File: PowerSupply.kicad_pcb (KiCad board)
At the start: 2 copper layers, 15 parts, among them J1 Barrel_Jack_Switch, J2 Conn_02x02_Odd_Even, J3 Conn_02x02_Odd_Even, SW1 SW_DPDT_x2, U1 LM7805_TO220

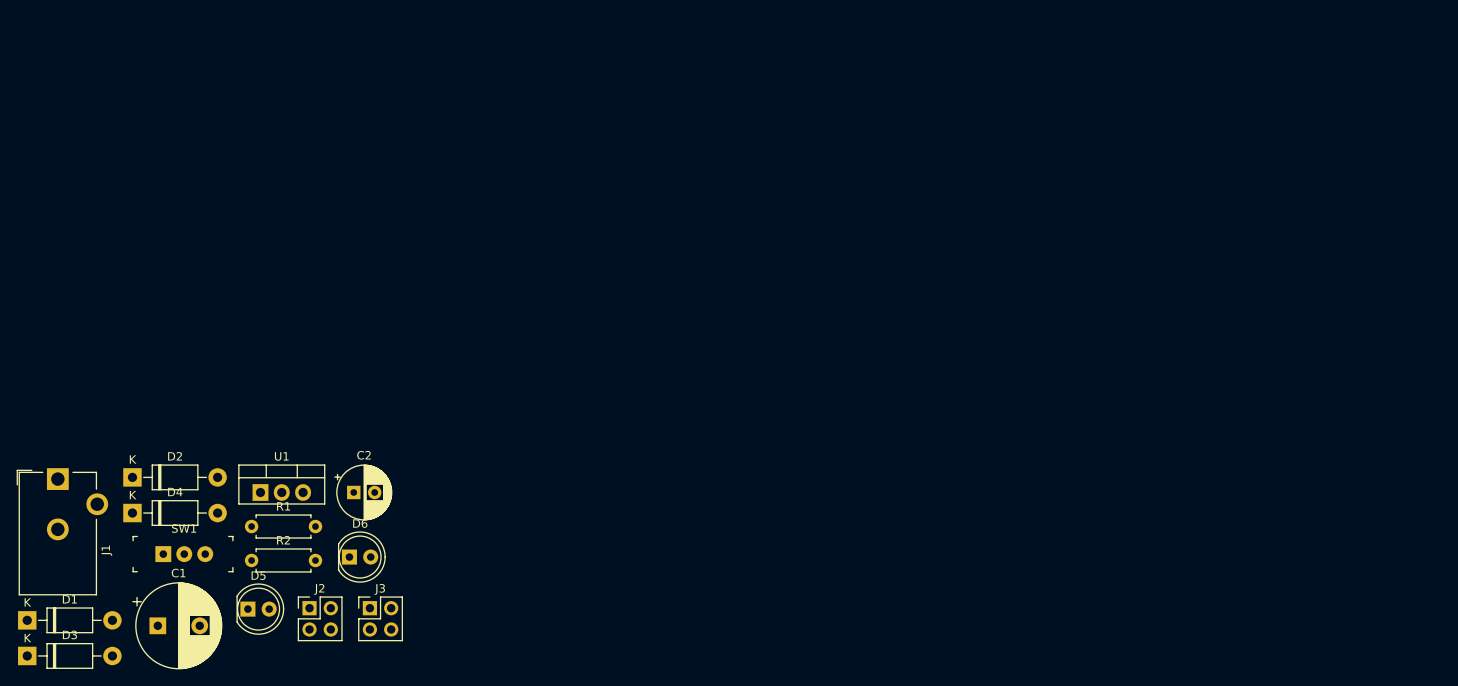
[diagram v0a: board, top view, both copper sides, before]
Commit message: Drew outline and constraints of the pcb
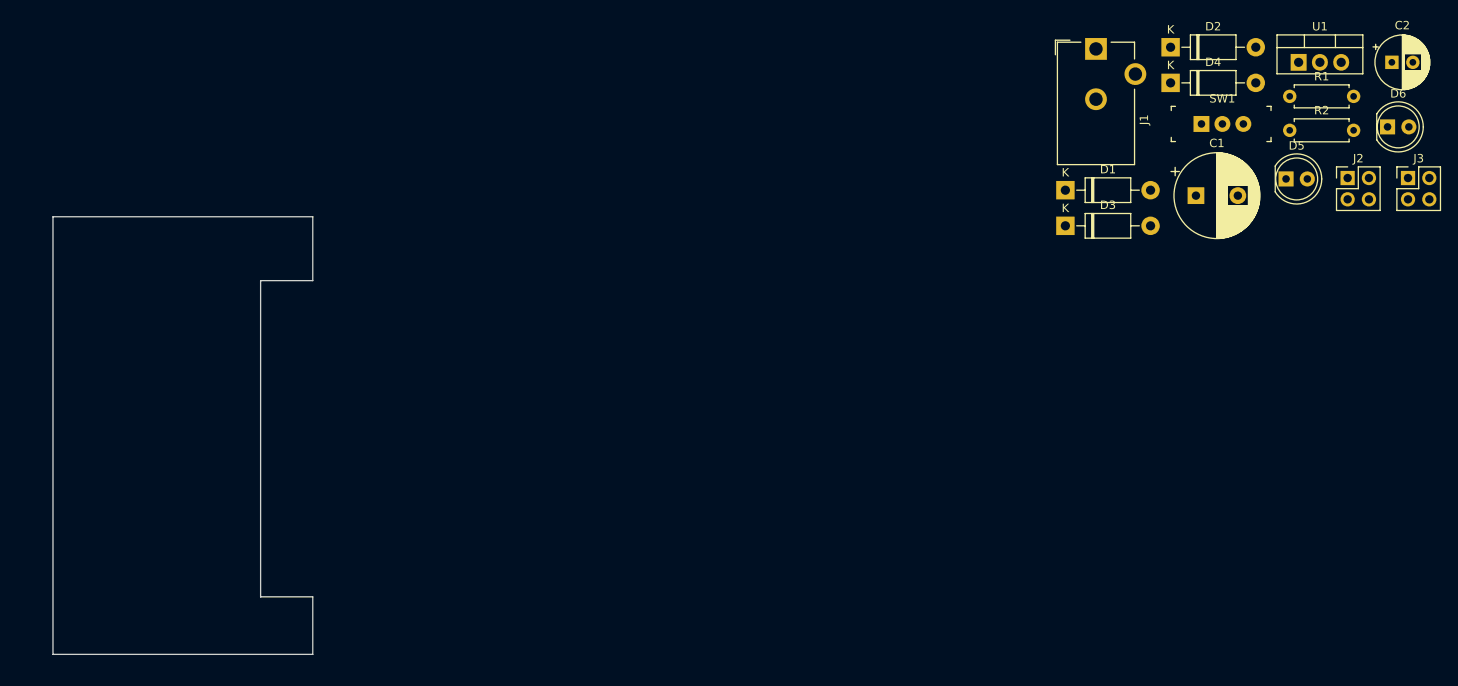
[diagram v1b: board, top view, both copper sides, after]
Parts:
- moved J2 134.0 mm to (256.4, 71.6)
- moved C1 134.0 mm to (238.3, 73.7)
- moved C2 134.0 mm to (261.7, 57.8)
- moved D1 134.0 mm to (222.7, 73.0)
- moved D2 134.0 mm to (235.3, 56.0)
- moved D3 134.0 mm to (222.7, 77.3)
- moved D4 134.0 mm to (235.3, 60.2)
- moved D5 134.0 mm to (249.1, 71.7)
- moved D6 134.0 mm to (261.2, 65.5)
- moved J1 134.0 mm to (226.4, 56.2)
- moved J3 134.0 mm to (263.6, 71.6)
- moved R1 134.0 mm to (249.5, 61.8)
- moved R2 134.0 mm to (249.5, 65.9)
- moved SW1 134.0 mm to (239.0, 65.1)
- moved U1 134.0 mm to (250.6, 57.8)
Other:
- board outline added: 31 x 52.2 mm
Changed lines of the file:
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@@
   (general
     (thickness 1.6)
-    (drawings 0)
+    (drawings 8)
     (tracks 0)
     (zones 0)
@@
   )
   (module Capacitor_THT:CP_Radial_D10.0mm_P5.00mm (layer F.Cu)
-    (at 114.485647 124.989001)
+    (at 238.310647 73.681001)
     (descr "CP, Radial series, Radial, pin pitch=5.00mm, , diameter=10mm, Electrolytic Capacitor")
     (tags "CP Radial series Radial pin pitch 5.00mm  diameter 10mm Electrolytic Capacitor")
@@
   )
   (module Capacitor_THT:CP_Radial_D6.3mm_P2.50mm (layer F.Cu)
-    (at 137.856242 109.089001)
+    (at 261.681242 57.781001)
     (descr "CP, Radial series, Radial, pin pitch=2.50mm, , diameter=6.3mm, Electrolytic Capacitor")
     (tags "CP Radial series Radial pin pitch 2.50mm  diameter 6.3mm Electrolytic Capacitor")
@@
   )
   (module Diode_THT:D_DO-41_SOD81_P10.16mm_Horizontal (layer F.Cu)
-    (at 98.911001 124.339001)
+    (at 222.736001 73.031001)
     (descr "Diode, DO-41_SOD81 series, Axial, Horizontal, pin pitch=10.16mm, , length*diameter=5.2*2.7mm^2, , http://www.diodes.com/_files/packages/DO-41%20(Plastic).pdf")
     (tags "Diode DO-41_SOD81 series Axial Horizontal pin pitch 10.16mm  length 5.2mm diameter 2.7mm")
@@
   )
   (module Diode_THT:D_DO-41_SOD81_P10.16mm_Horizontal (layer F.Cu)
-    (at 111.461001 107.289001)
+    (at 235.286001 55.981001)
     (descr "Diode, DO-41_SOD81 series, Axial, Horizontal, pin pitch=10.16mm, , length*diameter=5.2*2.7mm^2, , http://www.diodes.com/_files/packages/DO-41%20(Plastic).pdf")
     (tags "Diode DO-41_SOD81 series Axial Horizontal pin pitch 10.16mm  length 5.2mm diameter 2.7mm")
@@
   )
   (module Diode_THT:D_DO-41_SOD81_P10.16mm_Horizontal (layer F.Cu)
-    (at 98.911001 128.589001)
+    (at 222.736001 77.281001)
     (descr "Diode, DO-41_SOD81 series, Axial, Horizontal, pin pitch=10.16mm, , length*diameter=5.2*2.7mm^2, , http://www.diodes.com/_files/packages/DO-41%20(Plastic).pdf")
     (tags "Diode DO-41_SOD81 series Axial Horizontal pin pitch 10.16mm  length 5.2mm diameter 2.7mm")
@@
   )
   (module Diode_THT:D_DO-41_SOD81_P10.16mm_Horizontal (layer F.Cu)
-    (at 111.461001 111.539001)
+    (at 235.286001 60.231001)
     (descr "Diode, DO-41_SOD81 series, Axial, Horizontal, pin pitch=10.16mm, , length*diameter=5.2*2.7mm^2, , http://www.diodes.com/_files/packages/DO-41%20(Plastic).pdf")
     (tags "Diode DO-41_SOD81 series Axial Horizontal pin pitch 10.16mm  length 5.2mm diameter 2.7mm")
@@
   )
   (module LED_THT:LED_D5.0mm (layer F.Cu)
-    (at 125.231001 122.999001)
+    (at 249.056001 71.691001)
     (descr "LED, diameter 5.0mm, 2 pins, http://cdn-reichelt.de/documents/datenblatt/A500/LL-504BC2E-009.pdf")
     (tags "LED diameter 5.0mm 2 pins")
@@
   )
   (module LED_THT:LED_D5.0mm (layer F.Cu)
-    (at 137.341001 116.789001)
+    (at 261.166001 65.481001)
     (descr "LED, diameter 5.0mm, 2 pins, http://cdn-reichelt.de/documents/datenblatt/A500/LL-504BC2E-009.pdf")
     (tags "LED diameter 5.0mm 2 pins")
@@
   )
   (module Connector_BarrelJack:BarrelJack_CUI_PJ-102AH_Horizontal (layer F.Cu)
-    (at 102.561001 107.489001)
+    (at 226.386001 56.181001)
     (descr "Thin-pin DC Barrel Jack, https://cdn-shop.adafruit.com/datasheets/21mmdcjackDatasheet.pdf")
     (tags "Power Jack")
@@
   )
   (module Connector_PinHeader_2.54mm:PinHeader_2x02_P2.54mm_Vertical (layer F.Cu)
-    (at 132.581001 122.889001)
+    (at 256.406001 71.581001)
     (descr "Through hole straight pin header, 2x02, 2.54mm pitch, double rows")
     (tags "Through hole pin header THT 2x02 2.54mm double row")
@@
   )
   (module Connector_PinHeader_2.54mm:PinHeader_2x02_P2.54mm_Vertical (layer F.Cu)
-    (at 139.781001 122.889001)
+    (at 263.606001 71.581001)
     (descr "Through hole straight pin header, 2x02, 2.54mm pitch, double rows")
     (tags "Through hole pin header THT 2x02 2.54mm double row")
@@
   )
   (module Resistor_THT:R_Axial_DIN0207_L6.3mm_D2.5mm_P7.62mm_Horizontal (layer F.Cu)
-    (at 125.671001 113.149001)
+    (at 249.496001 61.841001)
     (descr "Resistor, Axial_DIN0207 series, Axial, Horizontal, pin pitch=7.62mm, 0.25W = 1/4W, length*diameter=6.3*2.5mm^2, http://cdn-reichelt.de/documents/datenblatt/B400/1_4W%23YAG.pdf")
     (tags "Resistor Axial_DIN0207 series Axial Horizontal pin pitch 7.62mm 0.25W = 1/4W length 6.3mm diameter 2.5mm")
@@
   )
   (module Resistor_THT:R_Axial_DIN0207_L6.3mm_D2.5mm_P7.62mm_Horizontal (layer F.Cu)
-    (at 125.671001 117.199001)
+    (at 249.496001 65.891001)
     (descr "Resistor, Axial_DIN0207 series, Axial, Horizontal, pin pitch=7.62mm, 0.25W = 1/4W, length*diameter=6.3*2.5mm^2, http://cdn-reichelt.de/documents/datenblatt/B400/1_4W%23YAG.pdf")
     (tags "Resistor Axial_DIN0207 series Axial Horizontal pin pitch 7.62mm 0.25W = 1/4W length 6.3mm diameter 2.5mm")
@@
   )
   (module digikey-footprints:Switch_Slide_11.6x4mm_EG1218 (layer F.Cu)
-    (at 115.141001 116.439001)
+    (at 238.966001 65.131001)
     (descr http://spec_sheets.e-switch.com/specs/P040040.pdf)
     (fp_text reference SW1 (at 2.49 -3.02) (layer F.SilkS)
@@
   )
   (module Package_TO_SOT_THT:TO-220-3_Vertical (layer F.Cu)
-    (at 126.731001 109.089001)
+    (at 250.556001 57.781001)
     (descr "TO-220-3, Vertical, RM 2.54mm, see https://www.vishay.com/docs/66542/to-220-1.pdf")
     (tags "TO-220-3 Vertical RM 2.54mm")
@@
     )
   )
+  (gr_line (start 132.969 76.2) (end 101.981 76.2) (layer Edge.Cuts) (width 0.05))
+  (gr_line (start 132.969 83.82) (end 132.969 76.2) (layer Edge.Cuts) (width 0.05))
+  (gr_line (start 126.746 83.82) (end 132.969 83.82) (layer Edge.Cuts) (width 0.05))
+  (gr_line (start 126.746 121.539) (end 126.746 83.82) (layer Edge.Cuts) (width 0.05))
+  (gr_line (start 132.969 121.539) (end 126.746 121.539) (layer Edge.Cuts) (width 0.05))
+  (gr_line (start 132.969 128.397) (end 132.969 121.539) (layer Edge.Cuts) (width 0.05))
+  (gr_line (start 101.981 128.397) (end 132.969 128.397) (layer Edge.Cuts) (width 0.05))
+  (gr_line (start 101.981 76.2) (end 101.981 128.397) (layer Edge.Cuts) (width 0.05))
 )

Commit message: placed the components on the pcb layout
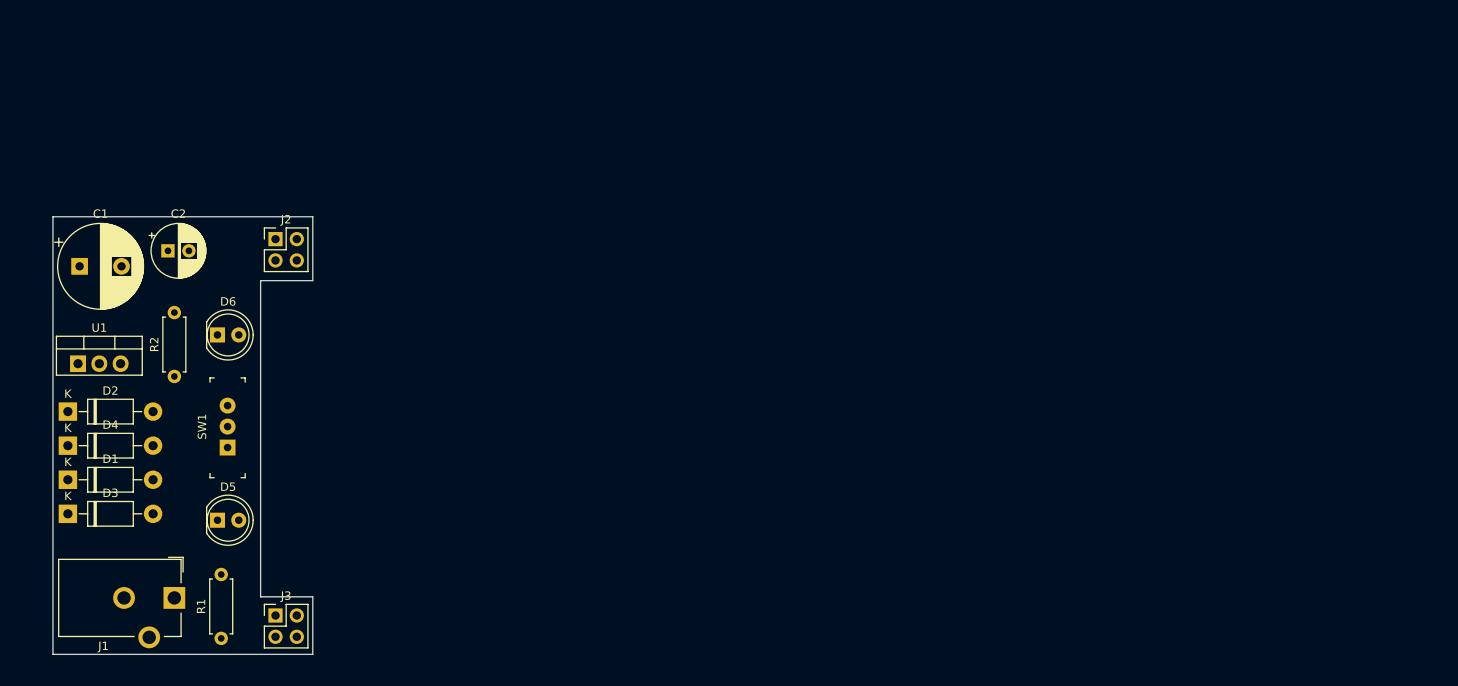
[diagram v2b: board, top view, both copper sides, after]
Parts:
- moved U1 150.0 mm to (105.0, 93.7)
- moved C2 147.7 mm to (115.7, 80.3)
- moved J3 144.8 mm to (128.5, 123.8)
- moved R1 142.9 mm to (122.0, 126.5), turned to 90 degrees
- moved D6 141.8 mm to (121.6, 90.3)
- moved D2 138.5 mm to (103.8, 99.4)
- moved D4 138.5 mm to (103.8, 103.5)
- moved R2 136.2 mm to (116.5, 95.2), turned to 90 degrees
- moved D5 133.8 mm to (121.6, 112.4)
- moved C1 133.4 mm to (105.2, 82.1)
- moved J2 128.1 mm to (128.5, 78.9)
- moved J1 128.0 mm to (116.5, 121.7), turned to 270 degrees
- moved D1 123.9 mm to (103.8, 107.6)
- moved D3 123.8 mm to (103.8, 111.6)
- moved SW1 122.4 mm to (122.8, 103.7), turned to 90 degrees

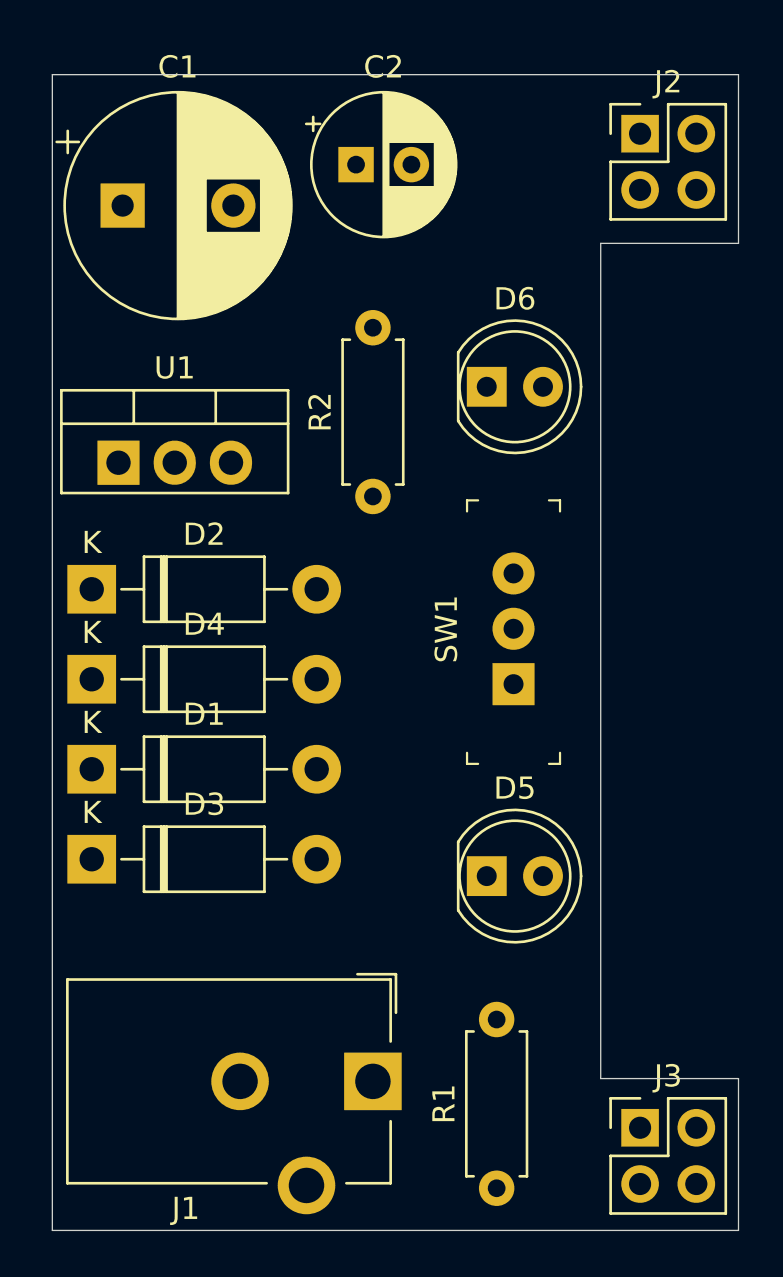
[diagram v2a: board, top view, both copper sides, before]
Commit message: Finished silkscreen
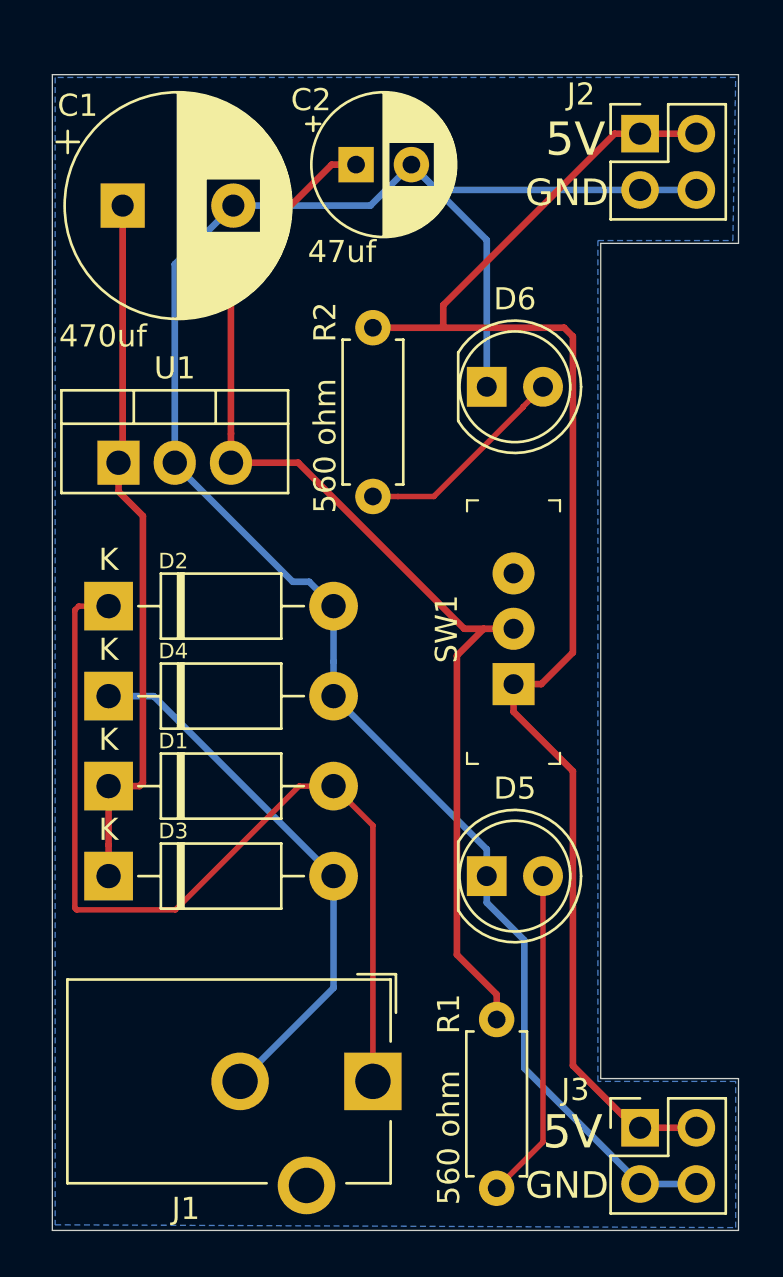
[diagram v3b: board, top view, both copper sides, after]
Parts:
- added G***: LOGO, KiCad Graphics:3HitComboLogoInverted, B.Cu at (109.6, 106.9)
- added REF**: KiCad-Logo2_8mm_SilkScreen, Symbol:KiCad-Logo2_8mm_SilkScreen, B.Cu at (115.4, 82.5)
- added REF**: OSHW-Logo2_7.3x6mm_SilkScreen, Symbol:OSHW-Logo2_7.3x6mm_SilkScreen, B.Cu at (108.5, 89.5)
- moved D1 1.08 mm to (104.5, 108.3)
- moved D2 1.08 mm to (104.5, 100.2)
- moved D3 1.08 mm to (104.5, 112.4)
- moved D4 1.08 mm to (104.5, 104.3)
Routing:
- net /V-: track 0.00 -> 90.6 mm
- net /Vout2: track 0.00 -> 67.9 mm
- net /Vout1: track 0.00 -> 51.2 mm
- net Net-(D1-Pad2): track 0.00 -> 43.2 mm
- net /Vin: track 0.00 -> 32.3 mm
- net Net-(D3-Pad2): track 0.00 -> 24.5 mm
- net Net-(D5-Pad2): track 0.00 -> 15.0 mm
- net Net-(D6-Pad2): track 0.00 -> 9.75 mm
- added copper zone on B.Cu, net /V-
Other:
- board text added: "470uf"
- board text added: "47uf"
- board text added: "560 ohm"
- board text added: "5V"
- board text added: "Breadboard Power Supply V1.0"
- board text added: "GND"
- board text added: "iRootAndCode.com"
